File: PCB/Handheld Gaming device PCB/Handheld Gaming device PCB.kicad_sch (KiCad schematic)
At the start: 36 parts, among them J1 Conn_02x20_Odd_Even, J12 FCC Connector Right Board, J13 FCC Connector Left Board, J2 USB_C_Receptacle_USB2.0_14P, J5 Display_5V, J6 Speaker, J7 AudioJack3_3.5mm, SW1 SW_SPDT, U1 TP4056-42-ESOP8, U2 MT3608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

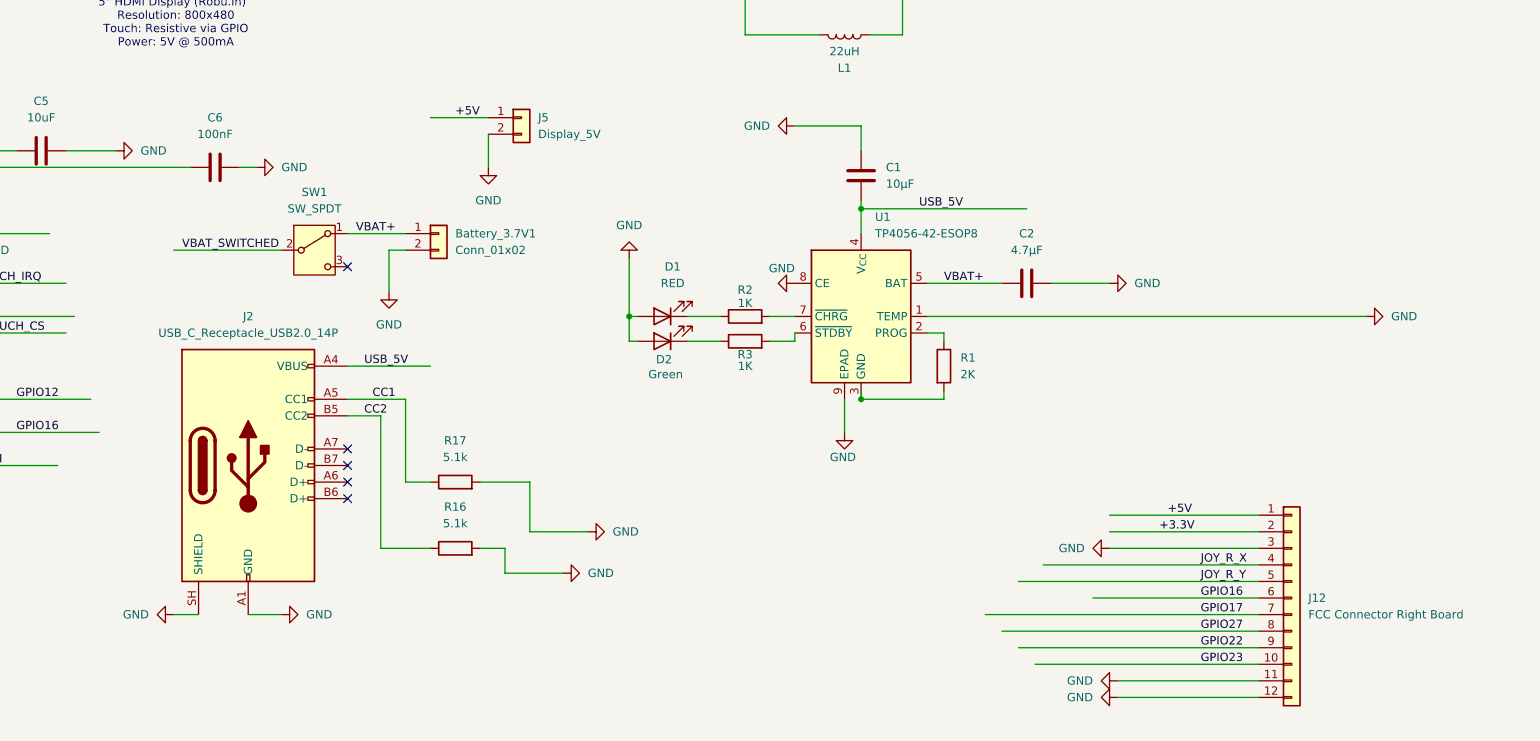
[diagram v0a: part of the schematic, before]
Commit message: changed the PCB to use the module instead of the chip
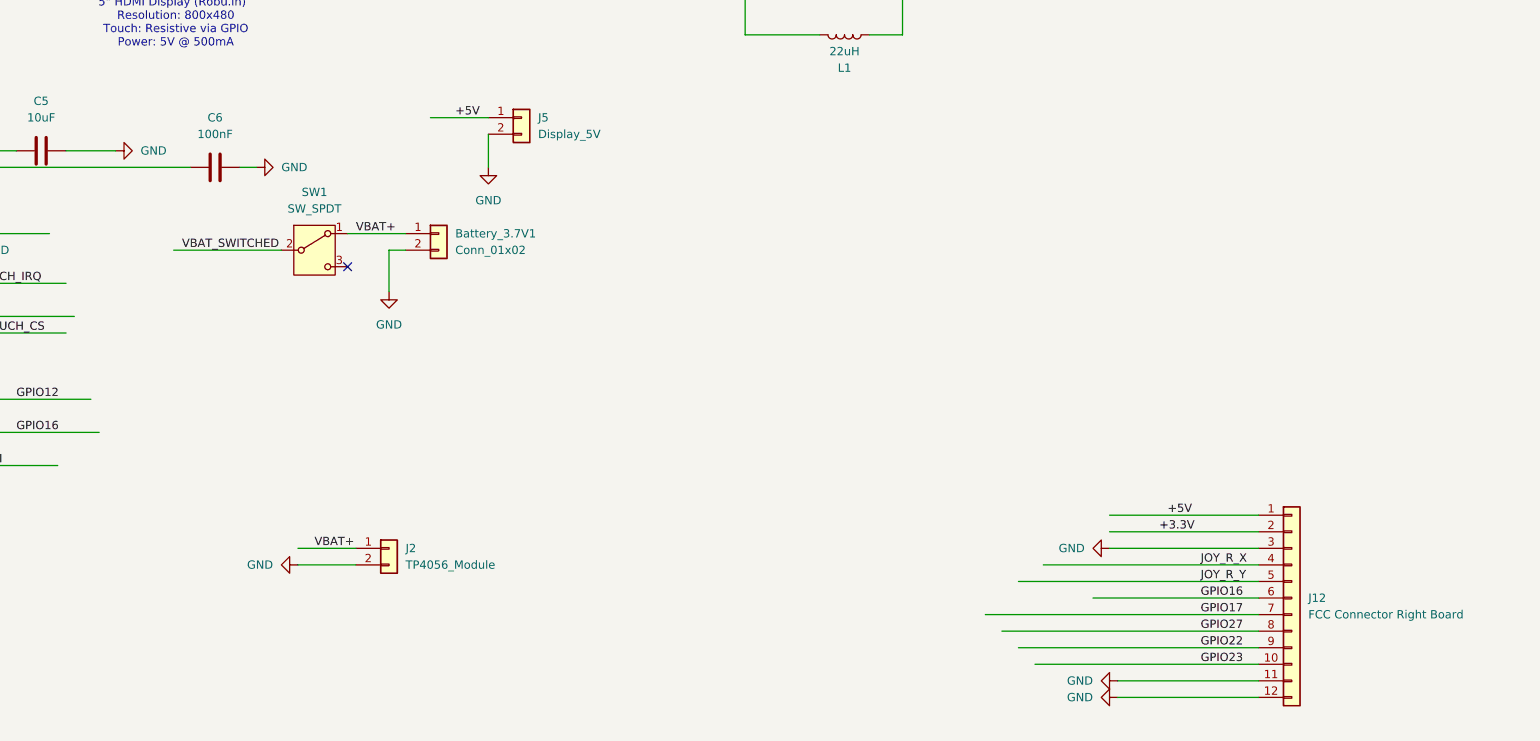
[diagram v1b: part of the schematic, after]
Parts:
- removed C1: 10µF, Capacitor_SMD:C_0805_2012Metric, symbol Device:C
- removed C2: 4.7µF, Capacitor_SMD:C_0805_2012Metric, symbol Device:C
- removed D1: RED, LED_THT:LED_D3.0mm, symbol Device:LED
- removed D2: Green, LED_THT:LED_D3.0mm, symbol Device:LED
- removed J2: USB_C_Receptacle_USB2.0_14P, Connector_USB:USB_C_Receptacle_GCT_USB4085, symbol Connector:USB_C_Receptacle_USB2.0_14P
- removed R1: 2K, Resistor_SMD:R_0402_1005Metric, symbol Device:R
- removed R16, R17: 5.1k, Resistor_SMD:R_0402_1005Metric, symbol Device:R
- removed R2, R3: 1K, Resistor_SMD:R_0402_1005Metric, symbol Device:R
- removed U1: TP4056-42-ESOP8, Package_SO:SOIC-8-1EP_3.9x4.9mm_P1.27mm_EP2.41x3.3mm_ThermalVias, symbol Battery_Management:TP4056-42-ESOP8
- added J2: TP4056_Module, Connector_PinHeader_2.54mm:PinHeader_1x02_P2.54mm_Vertical, symbol Connector_Generic:Conn_01x02
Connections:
- net GND: now also J2.2 (Pin_2)
- net VBAT+: now also J2.1 (Pin_1)
- no-connect marks 15 -> 11
